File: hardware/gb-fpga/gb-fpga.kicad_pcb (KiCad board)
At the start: 4 copper layers, 80.1 x 78.6 mm, 51 parts, among them J1 USB_C_Receptacle_USB2.0, J2 Cartridge-32pin, U1 xc7s25ftgb196, U2 MX25R3235FZBxx1, U3 FT2232HQ, U4 LTC3555, X1 SG-8002JA

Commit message: Update power circuit
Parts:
- added C11: 22µF, Capacitor_SMD:C_0603_1608Metric, F.Cu at (21.4, -2.20)
- added J3: BAT+, Connector_PinHeader_2.54mm:PinHeader_1x01_P2.54mm_Vertical, F.Cu at (12.0, -2.80)
- added J4: BAT-, Connector_PinHeader_2.54mm:PinHeader_1x01_P2.54mm_Vertical, F.Cu at (16.6, -2.80)
- added L4: 3.3µH, Inductor_SMD:L_0603_1608Metric, F.Cu at (20.2, -74.6)
- added R26: 10k, Resistor_SMD:R_0603_1608Metric, F.Cu at (32.0, -61.5)
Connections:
- U4 pad 1: Net-(U4-Pad1) -> Net-(C11-Pad1)
- U4 pad 11: Net-(U4-Pad1) -> VOUT
- U4 pad 13: USB_5V -> VOUT
- U4 pad 16: USB_5V -> VOUT
- U4 pad 18: Net-(U4-Pad1) -> VOUT
- U4 pad 24: Net-(U4-Pad1) -> Net-(C11-Pad1)
- U4 pad 27: USB_5V -> VOUT
- U4 pad 28: USB_5V -> VOUT
- U4 pad 5: Net-(U4-Pad1) -> VOUT
- U4 pad 7: USB_5V -> VOUT

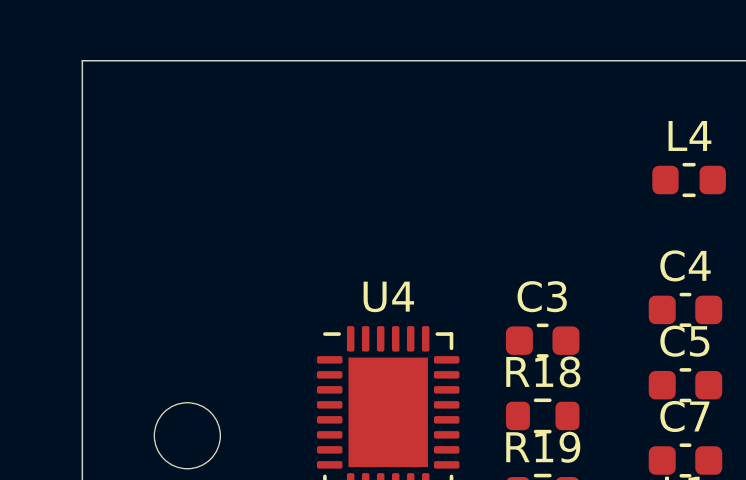
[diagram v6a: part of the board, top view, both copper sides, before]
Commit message: Use power up sequence recommended for Spartan FPGA
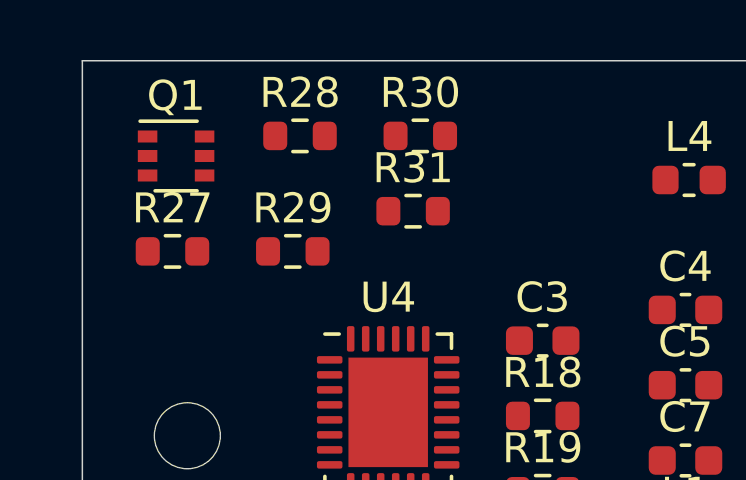
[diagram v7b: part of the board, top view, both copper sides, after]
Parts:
- added Q1: MBT3904DW1, Package_TO_SOT_SMD:SOT-363_SC-70-6, F.Cu at (3.13, -75.4)
- added R27: 3k, Resistor_SMD:R_0603_1608Metric, F.Cu at (3.01, -72.2)
- added R28: 10k, Resistor_SMD:R_0603_1608Metric, F.Cu at (7.26, -76.1)
- added R29: 30k, Resistor_SMD:R_0603_1608Metric, F.Cu at (7.02, -72.2)
- added R30: 30k, Resistor_SMD:R_0603_1608Metric, F.Cu at (11.3, -76.1)
- added R31: 1k, Resistor_SMD:R_0603_1608Metric, F.Cu at (11.0, -73.6)
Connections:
- U4 pad 13: VOUT -> Net-(R27-Pad2)
- U4 pad 7: VOUT -> Net-(Q1-Pad6)

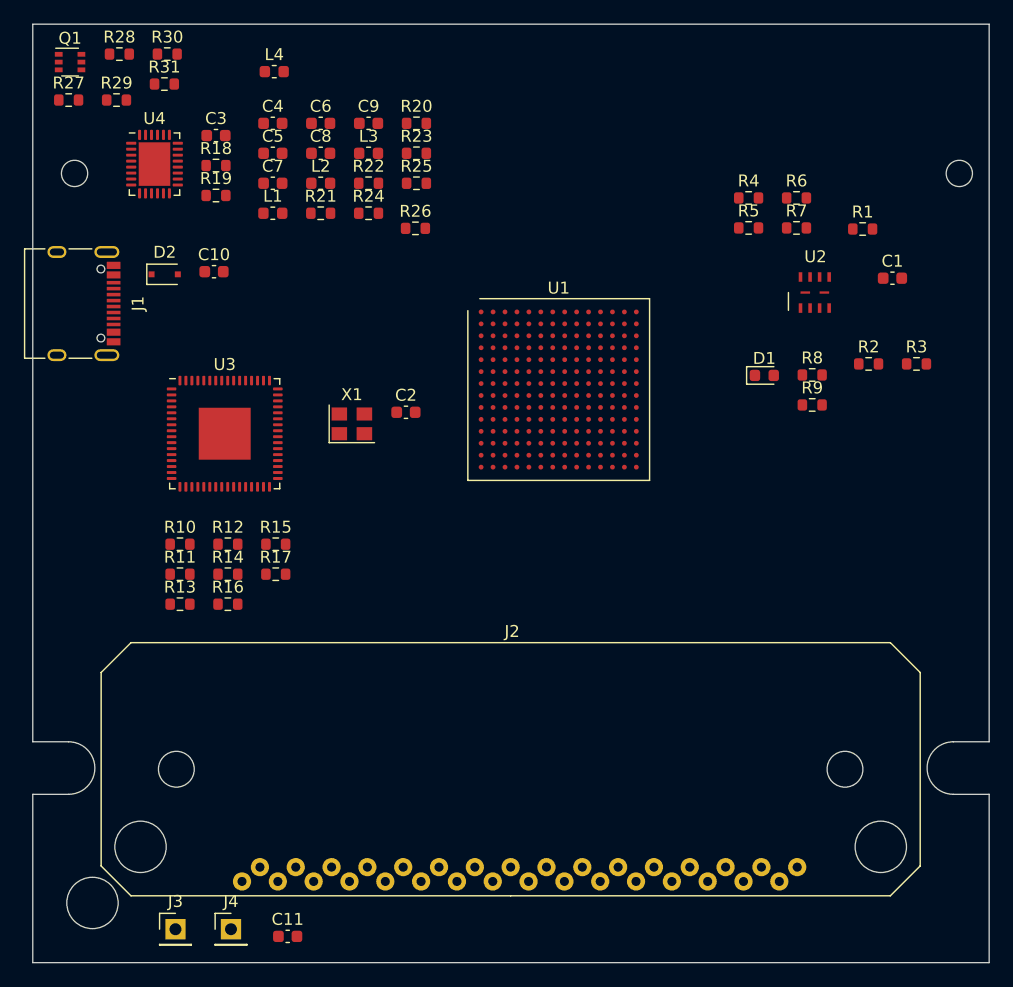
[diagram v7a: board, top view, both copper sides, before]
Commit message: Switch from 0603 to 0402 footprints
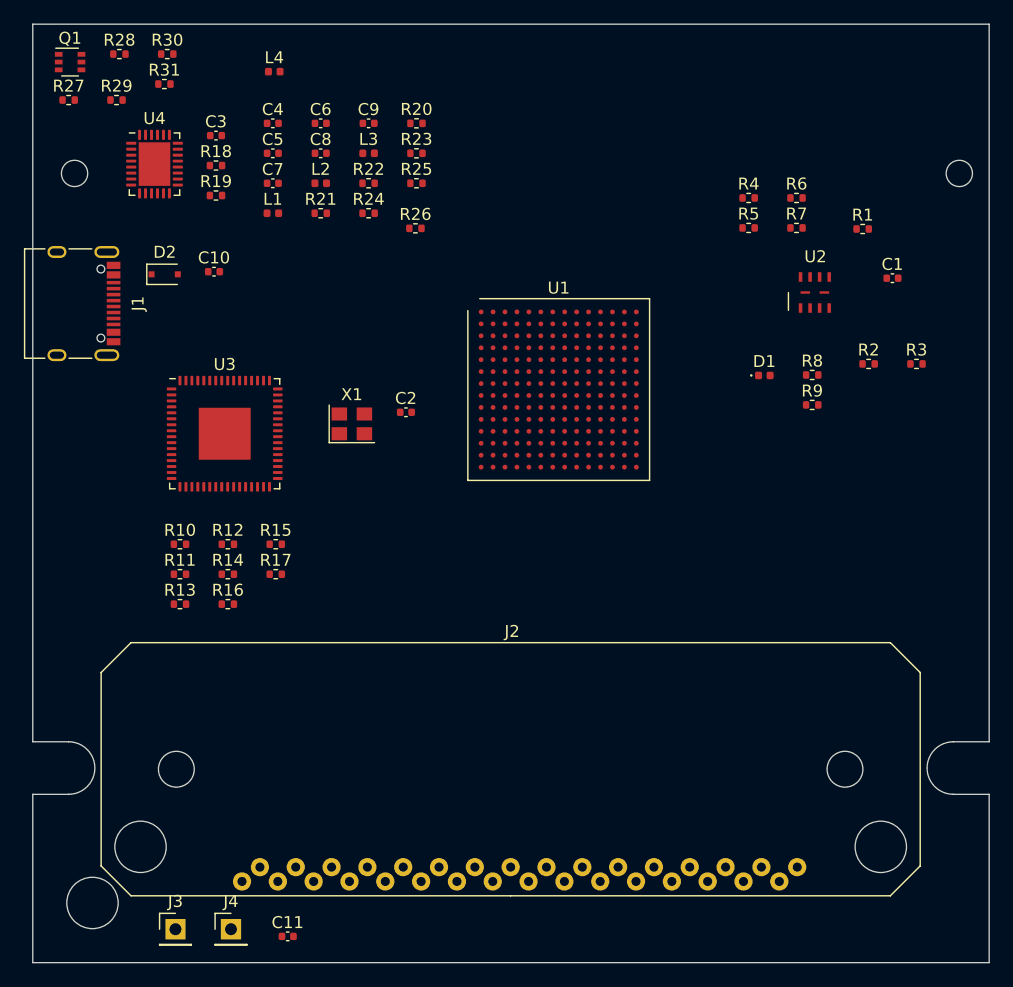
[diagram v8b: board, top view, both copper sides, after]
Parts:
- C1, C10, C11, C2, C3, C4, C5, C6, C7, C8, C9: footprint Capacitor_SMD:C_0603_1608Metric -> Capacitor_SMD:C_0402_1005Metric
- D1: footprint LED_SMD:LED_0603_1608Metric -> LED_SMD:LED_0402_1005Metric
- L1, L2, L3, L4: footprint Inductor_SMD:L_0603_1608Metric -> Inductor_SMD:L_0402_1005Metric
- R1, R10, R11, R12, R13, R14, R15, R16, R17, R18, R19, R2, R20, R21, R22, R23, R24, R25, R26, R27, R28, R29, R3, R30, R31, R4, R5, R6, R7, R8, R9: footprint Resistor_SMD:R_0603_1608Metric -> Resistor_SMD:R_0402_1005Metric
